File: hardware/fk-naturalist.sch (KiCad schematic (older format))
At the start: 99 parts, among them J1 MICRO-USB, J2 CONN_01X03, J3 CONN_01X06, J4 Conn_01x02, J5 Conn_01x01, J6 CONN-HDR-2x5, J7 Conn_01x01, J8 Conn_01x01, J9 Conn_01x01, M1 MOUNT_HOLE, M2 MOUNT_HOLE, M3 MOUNT_HOLE, M4 MOUNT_HOLE, Q1 2N7002LT1G, Q2 2N7002LT1G, Q3 2N7002LT1G, Q4 2N7002LT1G, SW1 SPNO, U1 ATSAMD21G18A-AU, U101 TSL2591, U102 MPL3115A2, U103 BNO055, U104 SHT31, U2 MCP1700T-XXX2E, U3 MAX4466, U4 S25FL1xxK0XM, Y1 FC-135, Y101 FC-135

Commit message: Renaming.
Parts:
- U103: symbol BNO055-RESCUE-fk-weather -> BNO055-RESCUE-fk-naturalist
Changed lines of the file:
@@
 EESchema Schematic File Version 2
-LIBS:fk-weather-rescue
+LIBS:fk-naturalist-rescue
 LIBS:conn
 LIBS:conservify
 LIBS:RocketScreamKicadLibrary
-LIBS:fk-weather-cache
+LIBS:fk-naturalist-cache
 EELAYER 25 0
 EELAYER END
@@
 $EndComp
 $Comp
-L BNO055-RESCUE-fk-weather U103
+L BNO055-RESCUE-fk-naturalist U103
 U 1 1 59784302
 P 9850 4700

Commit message: Expose Wire1 and Wire3 on header. Got rid of unnecessary jumpers.
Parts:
- removed J3: CONN_01X06, Socket_Strips:Socket_Strip_Straight_1x06_Pitch2.54mm, symbol CONN_01X06
- removed J7, J9: Conn_01x01, Measurement_Points:Measurement_Point_Round-SMD-Pad_Small, symbol Conn_01x01
- removed R18, R19, R20, R21, R22, R23, R24, R25: 0R, conservify:SJ_SHORTED, symbol RESISTOR
- added J3: Conn_01x08, Socket_Strips:Socket_Strip_Straight_1x08_Pitch2.54mm, symbol Conn_01x08
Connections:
- net labels removed: D11, D3, D4
- wire segments 300 -> 293
- no-connect marks 15 -> 14
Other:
- moved on the sheet: C109, D1, R1, U104

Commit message: Adding D30 and D31 to header.
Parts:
- removed J3: Conn_01x08, Socket_Strips:Socket_Strip_Straight_1x08_Pitch2.54mm, symbol Conn_01x08
- added J3: Conn_01x10, Socket_Strips:Socket_Strip_Straight_1x10_Pitch2.54mm, symbol Conn_01x10
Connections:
- wire segments 293 -> 295
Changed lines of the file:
@@
 Text Label 2100 3550 0    50   ~ 0
 SDA2
-$Comp
-L Conn_01x08 J3
-U 1 1 5A480C01
-P 7300 2950
-F 0 "J3" H 7300 3350 50  0000 C CNN
-F 1 "Conn_01x08" H 7300 2450 50  0000 C CNN
-F 2 "Socket_Strips:Socket_Strip_Straight_1x08_Pitch2.54mm" H 7300 2950 50  0001 C CNN
-F 3 "" H 7300 2950 50  0001 C CNN
-	1    7300 2950
-	1    0    0    -1
-$EndComp
 Text Label 6850 3150 0    50   ~ 0
 SCL3
@@
 	7100 3250 6850 3250
 $Comp
-L GND #PWR070
+L GND #PWR069
 U 1 1 5A487102
 P 6650 3400
-F 0 "#PWR070" H 6650 3150 50  0001 C CNN
+F 0 "#PWR069" H 6650 3150 50  0001 C CNN
 F 1 "GND" H 6650 3250 50  0001 C CNN
 F 2 "" H 6650 3400 60  0000 C CNN
@@
 	6650 3350 6650 3400
 $Comp
-L VUSB #PWR?
+L VUSB #PWR070
 U 1 1 5A488302
 P 6400 2850
-F 0 "#PWR?" H 6400 2700 50  0001 C CNN
+F 0 "#PWR070" H 6400 2700 50  0001 C CNN
 F 1 "VUSB" H 6400 2990 50  0000 C CNN
 F 2 "" H 6400 2850 60  0000 C CNN
@@
 	1    0    0    -1
 $EndComp
+Text Label 6850 3450 0    50   ~ 0
+D30
+Text Label 6850 3550 0    50   ~ 0
+D31
+$Comp
+L Conn_01x10 J3
+U 1 1 5A46BC2D
+P 7300 3050
+F 0 "J3" H 7300 3550 50  0000 C CNN
+F 1 "Conn_01x10" H 7300 2450 50  0000 C CNN
+F 2 "Socket_Strips:Socket_Strip_Straight_1x10_Pitch2.54mm" H 7300 3050 50  0001 C CNN
+F 3 "" H 7300 3050 50  0001 C CNN
+	1    7300 3050
+	1    0    0    -1
+$EndComp
+Wire Wire Line
+	6850 3450 7100 3450
+Wire Wire Line
+	7100 3550 6850 3550
 $EndSCHEMATC

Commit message: Starting on the combined coreless board. Schematic is... done hopefully.
This includes the change to the new I2S chip.
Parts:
- removed C16: 10uF, Capacitors_SMD:C_0603_HandSoldering, symbol CAPACITOR-CERAMIC
- removed C17: 100pF, Capacitors_SMD:C_0603_HandSoldering, symbol CAPACITOR-CERAMIC
- removed D4: PRTR5V0U2X, RocketScreamKicadLibrary:SOT-143B, symbol PRTR5V0U2X
- removed J1: MICRO-USB, conservify:MICRO-USB, symbol MICRO-USB
- removed J2: CONN_01X03, Socket_Strips:Socket_Strip_Straight_1x03_Pitch2.54mm, symbol CONN_01X03
- removed J3: Conn_01x10, Socket_Strips:Socket_Strip_Straight_1x10_Pitch2.54mm, symbol Conn_01x10
- removed J4: Conn_01x02, Socket_Strips:Socket_Strip_Straight_2x01_Pitch2.54mm, symbol Conn_01x02
- removed J5, J8: Conn_01x01, Measurement_Points:Measurement_Point_Round-SMD-Pad_Small, symbol Conn_01x01
- removed J6: CONN-HDR-2x5, Socket_Strips:Socket_Strip_Straight_2x05_Pitch1.27mm_SMD, symbol CONN-HDR-2x5
- removed L3, L4: WE-CBF, Resistors_SMD:R_0603_HandSoldering, symbol Ferrite_Bead_Small
- removed M2: MOUNT_HOLE, RocketScreamKicadLibrary:HOLE_NPTH_2.2MM, symbol MOUNT_HOLE
- removed MK1: CMA-4544PF-W, Socket_Strips:Socket_Strip_Straight_1x02_Pitch2.54mm, symbol Microphone
- removed R13: 1k, Resistors_SMD:R_0603_HandSoldering, symbol RESISTOR
- removed R14, R15: 1M, Resistors_SMD:R_0603_HandSoldering, symbol RESISTOR
- removed R16: 22k, Resistors_SMD:R_0603_HandSoldering, symbol RESISTOR
- removed R28, R29, R6, R7: 4.7K, Resistors_SMD:R_0603_HandSoldering, symbol RESISTOR
- removed RV1: TC33X-2-104E (100K), conservify:BOURNS-TC33X-2, symbol POT
- removed U1: ATSAMD21G18A-AU, RocketScreamKicadLibrary:TQFP-48_7x7mm_Pitch0.5mm, symbol ATSAMD21G18A-AU
- removed U2: MCP1700T-XXX2E, RocketScreamKicadLibrary:SOT-89, symbol MCP1700T-XXX2E
- removed U3: MAX4466, conservify:SC70-5, symbol MAX4466
- removed U4: S25FL1xxK0XM, RocketScreamKicadLibrary:SOIC-8-N, symbol S25FL1xxK0XM
- added BT1: Battery_Cell, Connectors:CR1220, symbol Battery_Cell
- added C19, C20, C25: 4.7uF 10V X5R, RocketScreamKicadLibrary:CAP-0603, symbol CAPACITOR-CERAMIC
- added C21, C23, C27, C29: 1uF 10V X5R, RocketScreamKicadLibrary:CAP-0603, symbol CAPACITOR-CERAMIC
- added C22, C24: 10uF, Capacitors_SMD:C_0603_HandSoldering, symbol CAPACITOR-CERAMIC
- added C26: 100nF, RocketScreamKicadLibrary:CAP-0603, symbol CAPACITOR-CERAMIC
- added C28: 10nF, RocketScreamKicadLibrary:CAP-0603, symbol CAPACITOR-CERAMIC
- added C30: 100pF, RocketScreamKicadLibrary:CAP-0603, symbol CAPACITOR-CERAMIC
- added C31, C32: 10uF, RocketScreamKicadLibrary:CAP-0603, symbol CAPACITOR-CERAMIC
- added D10, D11: Red, RocketScreamKicadLibrary:LED-0603, symbol LED-SINGLE
- added D4: Orange, RocketScreamKicadLibrary:LED-0603, symbol LED-SINGLE
- added D6: Blue, RocketScreamKicadLibrary:LED-0603, symbol LED-SINGLE
- added D7: PMEG3020CPA, RocketScreamKicadLibrary:SOT-1016, symbol DIODE_DUAL_Schottky
- added D8: PRTR5V0U2X, RocketScreamKicadLibrary:SOT-143B, symbol PRTR5V0U2X
- added D9: Green, RocketScreamKicadLibrary:LED-0603, symbol LED-SINGLE
- added J1: CONN_01X06, Socket_Strips:Socket_Strip_Straight_1x06_Pitch2.54mm, symbol CONN_01X06
- added J10: S2B-PH-SM4-TB, RocketScreamKicadLibrary:S2B-PH-SM4-TB, symbol S2B-PH-SM4-TB
- added J11: RF-SMA-EDGE, RocketScreamKicadLibrary:RF-SMA-EDGE, symbol RF-SMA-EDGE
- added J5: Conn_01x03, conservify:Molex_CLIK-Mate_502382-0370_1x03_P1.25mm_Vertical, symbol Conn_01x03
- added J6: Conn_01x05, conservify:Molex_CLIK-Mate_502382-0570_1x05_P1.25mm_Vertical, symbol Conn_01x05
- added J7: CONN-HDR-2x5, conservify:HDR_2x5_Pitch1.27mm_SMD_JTAG_SWD, symbol CONN-HDR-2x5
- added J8: Conn_01x09, Socket_Strips:Socket_Strip_Straight_1x09_Pitch2.54mm, symbol Conn_01x09
- added J9: MICRO-USB, RocketScreamKicadLibrary:MICRO-USB, symbol MICRO-USB
- added L5: 22uH, conservify:WURTH_L_6.0x6.0, symbol INDUCTOR
- added M6: MOUNT_HOLE, RocketScreamKicadLibrary:HOLE_NPTH_2.2MM, symbol MOUNT_HOLE
- added M7: MICROSD, conservify:MICROSD, symbol MICROSD
- added R18, R19, R20, R25, R33: 2K2, RocketScreamKicadLibrary:RES-0603, symbol RESISTOR
- added R21: 1K18, RocketScreamKicadLibrary:RES-0603, symbol RESISTOR
- added R22: 46K4, RocketScreamKicadLibrary:RES-0603, symbol RESISTOR
- added R23: 100K, RocketScreamKicadLibrary:RES-0603, symbol RESISTOR
- added R24: 2K94, RocketScreamKicadLibrary:RES-0603, symbol RESISTOR
- added R30: 330R, RocketScreamKicadLibrary:RES-0603, symbol RESISTOR
- added R31: 1M, RocketScreamKicadLibrary:RES-0603, symbol RESISTOR
- added R32, R34: 10K, RocketScreamKicadLibrary:RES-0603, symbol RESISTOR
- added R35, R36, R42, R43: 4.7K, RocketScreamKicadLibrary:RES-0603, symbol RESISTOR
- added R37: 1k, Resistors_SMD:R_0603_HandSoldering, symbol RESISTOR
- added R38, R44: 100k, RocketScreamKicadLibrary:RES-0603, symbol RESISTOR
- added R39, R40: 1k, RocketScreamKicadLibrary:RES-0603, symbol RESISTOR
- added R41: 180R, RocketScreamKicadLibrary:RES-0603, symbol RESISTOR
- added R45: 22K1, RocketScreamKicadLibrary:RES-0603, symbol RESISTOR
- added SW2: SPNO, conservify:SW_SPST_WURTH_1, symbol TACT-SWITCH_2Pins
- added U1: ATWINC1500-MR210PA, conservify:ATMEL_ATWINC1500-MR210PA, symbol ATWINC1500-MR210PA
- added U10: FGPMMOPA6H, conservify:FGPMMOPA6H, symbol FGPMMOPA6H
- added U11: MAX1704XX, Housings_DFN_QFN:DFN-8-1EP_3x2mm_Pitch0.5mm, symbol MAX1704XX
- added U2: ATSAMD21G18A-AU, RocketScreamKicadLibrary:TQFP-48_7x7mm_Pitch0.5mm, symbol ATSAMD21G18A-AU
- added U3: SPH0645, conservify:SPH0645LM4H-B, symbol SPH0645
- added U4: 24AA02E64, TO_SOT_Packages_SMD:SOT-23-5_HandSoldering, symbol 24AA02E64
- added U5: S25FL116K0XMFI041, RocketScreamKicadLibrary:SOIC-8-N, symbol S25FL1xxK0XM
- added U6: BQ24074RGTT, RocketScreamKicadLibrary:QFN-16_3x3mm, symbol BQ24074
- added U7: PCF8523, RocketScreamKicadLibrary:SOIC-8-N, symbol PCF8523
- added U8: MCP1700T-3302E/MB, RocketScreamKicadLibrary:SOT-89, symbol MCP1700T-XXX2E
- added U9: ISL8541x, Housings_DFN_QFN:DFN-12-1EP_3x4mm_Pitch0.5mm, symbol ISL8541x
- added Y2: FC-135, RocketScreamKicadLibrary:ABS07, symbol CRYSTAL
- C1: value 18pF -> 4.7uF 10V X5R; footprint Capacitors_SMD:C_0603_HandSoldering -> RocketScreamKicadLibrary:CAP-0603; price 0 -> 0.71; spn1 581-06035A180J -> 581-0603ZD475MAT2A
- C10: value 4.7nF -> 4.7uF 10V X5R; footprint Capacitors_SMD:C_0603_HandSoldering -> RocketScreamKicadLibrary:CAP-0603; price 0 -> 0.71; spn1 80-C0603C472K9R -> 581-0603ZD475MAT2A
- C11: value 1uF -> 100nF; footprint Capacitors_SMD:C_0603_HandSoldering -> RocketScreamKicadLibrary:CAP-0603; price 0 -> 0.1; spn1 963-UMK107BJ105KA-T -> 81-GRM39X104K50D
- C12: value 1uF -> 1uF 50V X5R; footprint Capacitors_SMD:C_0603_HandSoldering -> RocketScreamKicadLibrary:CAP-0603; price 0 -> 0.32
- C13: value 0.1uF -> 1uF; spn1 81-GRM39X104K50D -> 963-UMK107BJ105KA-T
- C14: value 4.7uF 10V X5R -> 4.7nF 25V X7R; footprint Capacitors_SMD:C_0603_HandSoldering -> RocketScreamKicadLibrary:CAP-0603; price 0 -> 0.1; spn1 581-0603ZD475MAT2A -> 603-AC603KRX7R8BB472
- C15: value 0.01uF -> 220pF; spn1 80-C0603C103J3GEAUTO -> 77-VJ0603A221KXXCBC
- C18, C7, C8: footprint Capacitors_SMD:C_0603_HandSoldering -> RocketScreamKicadLibrary:CAP-0603; price 0 -> 0.1
- C2: value 18pF -> 100nF; footprint Capacitors_SMD:C_0603_HandSoldering -> RocketScreamKicadLibrary:CAP-0603; price 0 -> 0.1; spn1 581-06035A180J -> 81-GRM39X104K50D
- C3, C4: value 100nF -> 18pF; footprint Capacitors_SMD:C_0603_HandSoldering -> RocketScreamKicadLibrary:CAP-0603; price 0 -> 0.1; spn1 81-GRM39X104K50D -> 581-06035A180J
- C5: value 1uF 10V X5R -> 100nF; footprint Capacitors_SMD:C_0603_HandSoldering -> RocketScreamKicadLibrary:CAP-0603; price 0 -> 0.1; spn1 581-0603YD105K -> 81-GRM39X104K50D
- C6: value 100nF -> 1uF 10V X5R; footprint Capacitors_SMD:C_0603_HandSoldering -> RocketScreamKicadLibrary:CAP-0603; price 0 -> 0.1; spn1 81-GRM39X104K50D -> 581-0603YD105K
- C9: value 4.7uF -> 100nF; footprint Capacitors_SMD:C_0603_HandSoldering -> RocketScreamKicadLibrary:CAP-0603; price 0 -> 0.1; spn1 581-0603ZD475MAT2A -> 81-GRM39X104K50D
- D1: price 0 -> 0.26
- D2: value Yellow -> Green; price 0 -> 0.28; spn1 859-LTST-C190KSKT -> 859-LTST-C190KGKT
- D3: value Blue -> Yellow; price 0 -> 0.3; spn1 859-LTST-C191TBKT -> 859-LTST-C190KSKT
- D5: value Orange -> Yellow; price 0 -> 0.3; spn1 859-LTST-C190KFKT -> 859-LTST-C190KSKT
- F1: price 0 -> 0.33
- L1, L2: footprint Inductors_SMD:L_0603_HandSoldering -> RocketScreamKicadLibrary:IND-0603; price 0 -> 0.1
- M1, M3, M4: price 0 -> (none)
- Q1, Q2, Q3, Q4: price 0 -> 0.14
- R1: value 2k2 -> 100k; footprint Resistors_SMD:R_0603_HandSoldering -> RocketScreamKicadLibrary:RES-0603; price 0 -> 0.1; spn1 603-RC0603FR-072K2L -> 603-RC0603FR-07100KL
- R10: value 1M -> 330R; footprint Resistors_SMD:R_0603_HandSoldering -> RocketScreamKicadLibrary:RES-0603; price 0 -> 0.1; spn1 603-RC0603FR-071ML -> 603-RC0603FR-07330RL
- R11: value 1k -> 10K; spn1 603-RC0603FR-071KL -> 603-RC0603FR-0710KL
- R12: value 1k -> 68R; spn1 603-RC0603FR-071KL -> 71-RCS060368R0FKEA
- R17: value 2k2 -> 10K; footprint Resistors_SMD:R_0603_HandSoldering -> RocketScreamKicadLibrary:RES-0603; price 0 -> 0.1; spn1 603-RC0603FR-072K2L -> 603-RC0603FR-0710KL
- R2: value 330R -> 100k; footprint Resistors_SMD:R_0603_HandSoldering -> RocketScreamKicadLibrary:RES-0603; price 0 -> 0.1; spn1 603-RC0603FR-07330RL -> 603-RC0603FR-07100KL
- R3: value 2k2 -> 2K2; footprint Resistors_SMD:R_0603_HandSoldering -> RocketScreamKicadLibrary:RES-0603; price 0 -> 0.1
- R4: value 10K -> 1k; footprint Resistors_SMD:R_0603_HandSoldering -> RocketScreamKicadLibrary:RES-0603; price 0 -> 0.1; spn1 603-RC0603FR-0710KL -> 603-RC0603FR-071KL
- R5: value 2k2 -> 1k; footprint Resistors_SMD:R_0603_HandSoldering -> RocketScreamKicadLibrary:RES-0603; price 0 -> 0.1; spn1 603-RC0603FR-072K2L -> 603-RC0603FR-071KL
- R8: value 100k -> 10K; footprint Resistors_SMD:R_0603_HandSoldering -> RocketScreamKicadLibrary:RES-0603; price 0 -> 0.1; spn1 603-RC0603FR-07100KL -> 603-RC0603FR-0710KL
- R9: footprint Resistors_SMD:R_0603_HandSoldering -> RocketScreamKicadLibrary:RES-0603; price 0 -> 0.1
- SW1: footprint RocketScreamKicadLibrary:TS-018 -> conservify:SW_SPST_WURTH_1; price 0 -> 0.55; supplier1 (none) -> digikey
- Y1: price 0 -> 0.54
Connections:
- net labels added: BAT_BACKUP, CHG, FLASH_CS, GPS_FIX, GPS_RX, GPS_TX, I2S_BCLK, I2S_DATA, I2S_WS, ISL_VIN, PG, RADIO_CS, RADIO_D0, RADIO_EN, RADIO_RST, SD_CS, USER_SW, VBAT, VBUS, VEXT, VIN, WIFI_CS, WIFI_EN, WIFI_IRQ, WIFI_RST, WIFI_WAKE
- net labels removed: A0, A1, A2, AGND, ATN, AVCC, D0, D1, D10, D12, D2, D5, D6, D7, D8, D9, RX_LED, SCL3, SDA3, TX_LED
- wire segments 295 -> 483
- no-connect marks 14 -> 39
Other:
- note added: "1. All capacitors are NP0/COG 50V unless specified.\n2. All resistors are 62.5mW 1% unless specified."
- note added: "100mA"
- note added: "16Mbit = 2Mbytes"
- note added: "24AA02E64 DEVICE ID\n"
- note added: "500mA"
- note added: "AUDIO"
- note added: "BNO055"
- note added: "BREAKOUT"
- note added: "EN2 EN1"
- note added: "GPS"
- note added: "HI HI"
- note added: "HI LOW"
- note added: "I-INPUT LIMIT"
- note added: "I2C PULLUP\n"
- note added: "LED"
- note added: "LEDS"
- note added: "LIPO GAUGE"
- note added: "LOW HI"
- note added: "LOW LOW"
- note added: "MCU"
- note added: "MOUNTING"
- note added: "MPL3115A2"
- note added: "NOTES"
- note added: "POWER MANAGEMENT"
- note added: "POWER MANAGEMENT (3V3 REGULATOR)"
- note added: "RFM95W\n"
- note added: "RTC"
- note added: "SD"
- note added: "SERIAL FLASH"
- note added: "SHT31"
- note added: "SWD/JTAG"
- note added: "Set by R6:1.3A"
- note added: "Standby"
- note added: "TSL2591"
- note added: "USB-DEVICE"
- note added: "VIN:5-10.5V\n(OVP up to 28V)"
- note added: "WIFI"
- moved on the sheet: C101, C102, C103, C104, C105, C106, C107, C108, C109, R101, R102, R103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

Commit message: Working on the new PCB layout.
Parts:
- removed C2: 100nF, RocketScreamKicadLibrary:CAP-0603, symbol CAPACITOR-CERAMIC
- removed J1: CONN_01X06, Socket_Strips:Socket_Strip_Straight_1x06_Pitch2.54mm, symbol CONN_01X06
- BT1: footprint Connectors:CR1220 -> conservify:BAT_CR1210
- C1: value 4.7uF 10V X5R -> 1uF; price 0.71 -> 0; spn1 581-0603ZD475MAT2A -> 963-UMK107BJ105KA-T
- C101, C102, C103, C104, C105, C106, C107, C108, C109, C13, C15, C22, C24: footprint Capacitors_SMD:C_0603_HandSoldering -> RocketScreamKicadLibrary:CAP-0603
- R101, R102, R103, R11, R12, R26, R27, R37: footprint Resistors_SMD:R_0603_HandSoldering -> RocketScreamKicadLibrary:RES-0603
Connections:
- wire segments 483 -> 466
- no-connect marks 39 -> 38

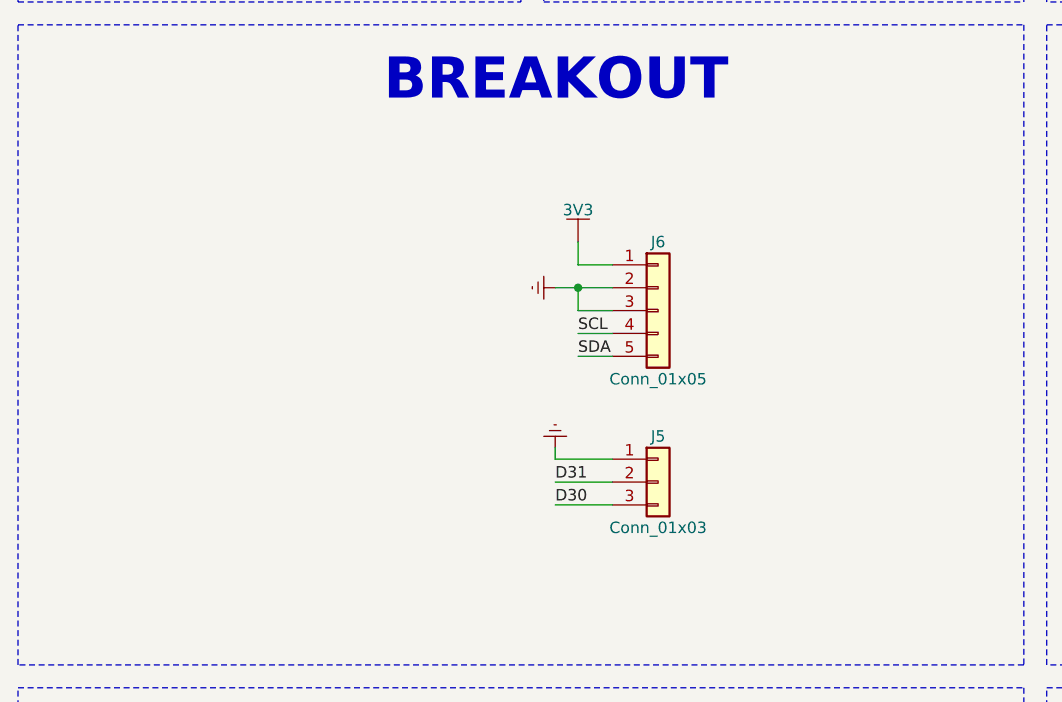
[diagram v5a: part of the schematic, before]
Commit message: Breakaway part for sensors.
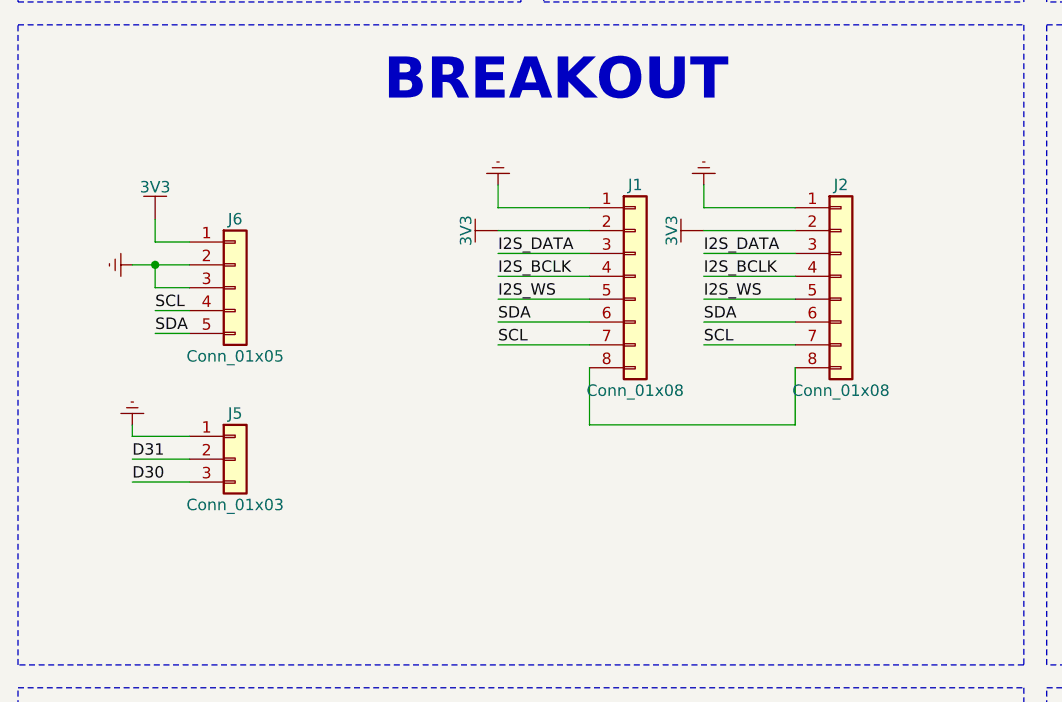
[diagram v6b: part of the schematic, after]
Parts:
- added J1, J2: Conn_01x08, Socket_Strips:Socket_Strip_Straight_1x08_Pitch2.54mm, symbol Conn_01x08
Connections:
- wire segments 466 -> 485
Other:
- moved on the sheet: J5, J6
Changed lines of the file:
@@
 L Conn_01x03 J5
 U 1 1 5A59629E
-P 3400 10300
-F 0 "J5" H 3400 10500 50  0000 C CNN
-F 1 "Conn_01x03" H 3400 10100 50  0000 C CNN
-F 2 "conservify:Molex_CLIK-Mate_502382-0370_1x03_P1.25mm_Vertical" H 3400 10300 50  0001 C CNN
-F 3 "" H 3400 10300 50  0001 C CNN
-F 4 "538-502382-0370" H 3400 10300 60  0001 C CNN "spn1"
-F 5 "mouser" H 3400 10300 60  0001 C CNN "supplier1"
-	1    3400 10300
+P 1550 10200
+F 0 "J5" H 1550 10400 50  0000 C CNN
+F 1 "Conn_01x03" H 1550 10000 50  0000 C CNN
+F 2 "conservify:Molex_CLIK-Mate_502382-0370_1x03_P1.25mm_Vertical" H 1550 10200 50  0001 C CNN
+F 3 "" H 1550 10200 50  0001 C CNN
+F 4 "538-502382-0370" H 1550 10200 60  0001 C CNN "spn1"
+F 5 "mouser" H 1550 10200 60  0001 C CNN "supplier1"
+	1    1550 10200
 	1    0    0    -1
 $EndComp
@@
 L GND #PWR0103
 U 1 1 5A59629F
-P 2950 10150
-F 0 "#PWR0103" H 2950 9900 50  0001 C CNN
-F 1 "GND" H 2950 10000 50  0001 C CNN
-F 2 "" H 2950 10150 60  0000 C CNN
-F 3 "" H 2950 10150 60  0000 C CNN
-	1    2950 10150
+P 1100 10050
+F 0 "#PWR0103" H 1100 9800 50  0001 C CNN
+F 1 "GND" H 1100 9900 50  0001 C CNN
+F 2 "" H 1100 10050 60  0000 C CNN
+F 3 "" H 1100 10050 60  0000 C CNN
+	1    1100 10050
 	-1   0    0    1
 $EndComp
-Text Label 2950 10300 0    50   ~ 0
+Text Label 1100 10200 0    50   ~ 0
 D31
-Text Label 2950 10400 0    50   ~ 0
+Text Label 1100 10300 0    50   ~ 0
 D30
 $Comp
 L Conn_01x05 J6
 U 1 1 5A5962A1
-P 3400 9550
-F 0 "J6" H 3400 9850 50  0000 C CNN
-F 1 "Conn_01x05" H 3400 9250 50  0000 C CNN
-F 2 "conservify:Molex_CLIK-Mate_502382-0570_1x05_P1.25mm_Vertical" H 3400 9550 50  0001 C CNN
-F 3 "" H 3400 9550 50  0001 C CNN
-F 4 "538-502382-0570" H 3400 9550 60  0001 C CNN "spn1"
-F 5 "mouser" H 3400 9550 60  0001 C CNN "supplier1"
-	1    3400 9550
-	1    0    0    -1
-$EndComp
-Text Label 3050 9750 0    50   ~ 0
+P 1550 9450
+F 0 "J6" H 1550 9750 50  0000 C CNN
+F 1 "Conn_01x05" H 1550 9150 50  0000 C CNN
+F 2 "conservify:Molex_CLIK-Mate_502382-0570_1x05_P1.25mm_Vertical" H 1550 9450 50  0001 C CNN
+F 3 "" H 1550 9450 50  0001 C CNN
+F 4 "538-502382-0570" H 1550 9450 60  0001 C CNN "spn1"
+F 5 "mouser" H 1550 9450 60  0001 C CNN "supplier1"
+	1    1550 9450
+	1    0    0    -1
+$EndComp
+Text Label 1200 9650 0    50   ~ 0
 SDA
-Text Label 3050 9650 0    50   ~ 0
+Text Label 1200 9550 0    50   ~ 0
 SCL
 $Comp
 L GND #PWR0104
 U 1 1 5A5962A2
-P 2950 9450
-F 0 "#PWR0104" H 2950 9200 50  0001 C CNN
-F 1 "GND" H 2950 9300 50  0001 C CNN
-F 2 "" H 2950 9450 60  0000 C CNN
-F 3 "" H 2950 9450 60  0000 C CNN
-	1    2950 9450
+P 1100 9350
+F 0 "#PWR0104" H 1100 9100 50  0001 C CNN
+F 1 "GND" H 1100 9200 50  0001 C CNN
+F 2 "" H 1100 9350 60  0000 C CNN
+F 3 "" H 1100 9350 60  0000 C CNN
+	1    1100 9350
 	0    1    1    0
 $EndComp
@@
 L 3V3 #PWR0105
 U 1 1 5A5962A3
-P 3050 9250
-F 0 "#PWR0105" H 3050 9100 50  0001 C CNN
-F 1 "3V3" H 3050 9390 50  0000 C CNN
-F 2 "" H 3050 9250 60  0000 C CNN
-F 3 "" H 3050 9250 60  0000 C CNN
-	1    3050 9250
+P 1200 9150
+F 0 "#PWR0105" H 1200 9000 50  0001 C CNN
+F 1 "3V3" H 1200 9290 50  0000 C CNN
+F 2 "" H 1200 9150 60  0000 C CNN
+F 3 "" H 1200 9150 60  0000 C CNN
+	1    1200 9150
 	1    0    0    -1
 $EndComp
@@
 	21400 9550 21400 9650
 Wire Wire Line
-	2950 10150 2950 10200
-Wire Wire Line
-	2950 10200 3200 10200
-Wire Wire Line
-	3200 10300 2950 10300
-Wire Wire Line
-	2950 10400 3200 10400
-Wire Wire Line
-	2950 9450 3200 9450
-Wire Wire Line
-	3050 9650 3200 9650
-Wire Wire Line
-	3050 9750 3200 9750
-Wire Wire Line
-	3200 9550 3050 9550
-Wire Wire Line
-	3050 9550 3050 9450
-Connection ~ 3050 9450
-Wire Wire Line
-	3200 9350 3050 9350
-Wire Wire Line
-	3050 9350 3050 9250
+	1100 10050 1100 10100
+Wire Wire Line
+	1100 10100 1350 10100
+Wire Wire Line
+	1350 10200 1100 10200
+Wire Wire Line
+	1100 10300 1350 10300
+Wire Wire Line
+	1100 9350 1350 9350
+Wire Wire Line
+	1200 9550 1350 9550
+Wire Wire Line
+	1200 9650 1350 9650
+Wire Wire Line
+	1350 9450 1200 9450
+Wire Wire Line
+	1200 9450 1200 9350
+Connection ~ 1200 9350
+Wire Wire Line
+	1350 9250 1200 9250
+Wire Wire Line
+	1200 9250 1200 9150
 Text Notes 8600 13150 0    180  ~ 36
 MPL3115A2
@@
 Wire Wire Line
 	900  2800 900  2950
+Text Label 2700 9600 0    50   ~ 0
+SDA
+Text Label 2700 9700 0    50   ~ 0
+SCL
+$Comp
+L GND #PWR0113
+U 1 1 5A5D8302
+P 2700 9000
+F 0 "#PWR0113" H 2700 8750 50  0001 C CNN
+F 1 "GND" H 2700 8850 50  0001 C CNN
+F 2 "" H 2700 9000 60  0000 C CNN
+F 3 "" H 2700 9000 60  0000 C CNN
+	1    2700 9000
+	-1   0    0    1
+$EndComp
+$Comp
+L 3V3 #PWR0114
+U 1 1 5A5D86A5
+P 2700 9200
+F 0 "#PWR0114" H 2700 9050 50  0001 C CNN
+F 1 "3V3" H 2700 9340 50  0000 C CNN
+F 2 "" H 2700 9200 60  0000 C CNN
+F 3 "" H 2700 9200 60  0000 C CNN
+	1    2700 9200
+	0    -1   -1   0
+$EndComp
+Text Label 2700 9300 0    50   ~ 0
+I2S_DATA
+Text Label 2700 9400 0    50   ~ 0
+I2S_BCLK
+Text Label 2700 9500 0    50   ~ 0
+I2S_WS
+Wire Wire Line
+	3100 9100 2700 9100
+Wire Wire Line
+	2700 9100 2700 9000
+Wire Wire Line
+	2700 9200 3100 9200
+Wire Wire Line
+	3100 9300 2700 9300
+Wire Wire Line
+	2700 9400 3100 9400
+Wire Wire Line
+	2700 9500 3100 9500
+Wire Wire Line
+	2700 9600 3100 9600
+Wire Wire Line
+	2700 9700 3100 9700
+Text Label 3600 9600 0    50   ~ 0
+SDA
+Text Label 3600 9700 0    50   ~ 0
+SCL
+$Comp
+L GND #PWR0115
+U 1 1 5A5E9714
+P 3600 9000
+F 0 "#PWR0115" H 3600 8750 50  0001 C CNN
+F 1 "GND" H 3600 8850 50  0001 C CNN
+F 2 "" H 3600 9000 60  0000 C CNN
+F 3 "" H 3600 9000 60  0000 C CNN
+	1    3600 9000
+	-1   0    0    1
+$EndComp
+$Comp
+L 3V3 #PWR0116
+U 1 1 5A5E971A
+P 3600 9200
+F 0 "#PWR0116" H 3600 9050 50  0001 C CNN
+F 1 "3V3" H 3600 9340 50  0000 C CNN
+F 2 "" H 3600 9200 60  0000 C CNN
+F 3 "" H 3600 9200 60  0000 C CNN
+	1    3600 9200
+	0    -1   -1   0
+$EndComp
+Text Label 3600 9300 0    50   ~ 0
+I2S_DATA
+Text Label 3600 9400 0    50   ~ 0
+I2S_BCLK
+Text Label 3600 9500 0    50   ~ 0
+I2S_WS
+$Comp
+L Conn_01x08 J2
+U 1 1 5A5E9723
+P 4200 9400
+F 0 "J2" H 4200 9800 50  0000 C CNN
+F 1 "Conn_01x08" H 4200 8900 50  0000 C CNN
+F 2 "Socket_Strips:Socket_Strip_Straight_1x08_Pitch2.54mm" H 4200 9400 50  0001 C CNN
+F 3 "" H 4200 9400 50  0001 C CNN
+	1    4200 9400
+	1    0    0    -1
+$EndComp
+Wire Wire Line
+	4000 9100 3600 9100
+Wire Wire Line
+	3600 9100 3600 9000
+Wire Wire Line
+	3600 9200 4000 9200
+Wire Wire Line
+	4000 9300 3600 9300
+Wire Wire Line
+	3600 9400 4000 9400
+Wire Wire Line
+	3600 9500 4000 9500
+Wire Wire Line
+	3600 9600 4000 9600
+Wire Wire Line
+	3600 9700 4000 9700
+$Comp
+L Conn_01x08 J1
+U 1 1 5A5DE4BD
+P 3300 9400
+F 0 "J1" H 3300 9800 50  0000 C CNN
+F 1 "Conn_01x08" H 3300 8900 50  0000 C CNN
+F 2 "Socket_Strips:Socket_Strip_Straight_1x08_Pitch2.54mm" H 3300 9400 50  0001 C CNN
+F 3 "" H 3300 9400 50  0001 C CNN
+	1    3300 9400
+	1    0    0    -1
+$EndComp
+Wire Wire Line
+	4000 9800 4000 10050
+Wire Wire Line
+	4000 10050 3100 10050
+Wire Wire Line
+	3100 10050 3100 9800
 $EndSCHEMATC
